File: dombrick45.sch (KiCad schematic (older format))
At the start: 5 parts

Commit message: 2019-10-04
2019-10-04 ai10さんブログの演習途中
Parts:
- added C1, C2: 22pF, Capacitor_SMD:C_0805_2012Metric, symbol Device:C_Small
- added C4, C5, C6: 0.1uF, Capacitor_SMD:C_0805_2012Metric, symbol Device:C_Small
- added C7: 10uF, Capacitor_SMD:C_0805_2012Metric, symbol Device:C_Small
- added D1, D2, D3, D4: SOD-123, Diode_SMD:D_SOD-123, symbol Device:D_Small
- added F1: 500mA, Fuse:Fuse_1206_3216Metric, symbol Device:Polyfuse_Small
- added MX1, MX2, MX3, MX4: MX-NoLED, MX_Alps_Hybrid:MX-1U-NoLED, symbol MX_Alps_Hybrid:MX-NoLED
- added R1: 10k, Resistor_SMD:R_0805_2012Metric, symbol Device:R_Small
- added SW1: SW_Push, symbol Switch:SW_Push
- added USB1: Molex-0548190589, symbol random-keyboard-parts:Molex-0548190589
- added Y1: 16MHz, symbol Device:Crystal_GND24_Small
- C3: renamed from C?; footprint (none) -> Capacitor_SMD:C_0805_2012Metric
- R2, R3, R4: renamed from R?; footprint (none) -> Resistor_SMD:R_0805_2012Metric
- gave numbers to parts that had none: 1
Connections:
- net labels added: COL0, COL1, D+, D-, ROW0, ROW1, VCC
- wire segments 13 -> 58
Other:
- moved on the sheet: R2, R3

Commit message: 2019-10-06
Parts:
- C1, C2, C3, C4, C5, C6, C7: footprint Capacitor_SMD:C_0805_2012Metric -> Capacitor_SMD:C_0805_2012Metric_Pad1.15x1.40mm_HandSolder
- SW1: footprint (none) -> random-keyboard-parts:SKQG-1155865
- USB1: footprint (none) -> random-keyboard-parts:Molex-0548190589
- Y1: footprint (none) -> Crystal:Crystal_SMD_3225-4Pin_3.2x2.5mm
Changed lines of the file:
@@
 F 0 "C3" H 2992 3271 50  0000 L CNN
 F 1 "1uF" H 2992 3180 50  0000 L CNN
-F 2 "Capacitor_SMD:C_0805_2012Metric" H 2900 3225 50  0001 C CNN
+F 2 "Capacitor_SMD:C_0805_2012Metric_Pad1.15x1.40mm_HandSolder" H 2900 3225 50  0001 C CNN
 F 3 "~" H 2900 3225 50  0001 C CNN
 	1    2900 3225
@@
 F 0 "C4" H 1892 4246 50  0000 L CNN
 F 1 "0.1uF" H 1892 4155 50  0000 L CNN
-F 2 "Capacitor_SMD:C_0805_2012Metric" H 1800 4200 50  0001 C CNN
+F 2 "Capacitor_SMD:C_0805_2012Metric_Pad1.15x1.40mm_HandSolder" H 1800 4200 50  0001 C CNN
 F 3 "~" H 1800 4200 50  0001 C CNN
 	1    1800 4200
@@
 F 0 "C5" H 2317 4246 50  0000 L CNN
 F 1 "0.1uF" H 2317 4155 50  0000 L CNN
-F 2 "Capacitor_SMD:C_0805_2012Metric" H 2225 4200 50  0001 C CNN
+F 2 "Capacitor_SMD:C_0805_2012Metric_Pad1.15x1.40mm_HandSolder" H 2225 4200 50  0001 C CNN
 F 3 "~" H 2225 4200 50  0001 C CNN
 	1    2225 4200
@@
 F 0 "C6" H 2742 4246 50  0000 L CNN
 F 1 "0.1uF" H 2742 4155 50  0000 L CNN
-F 2 "Capacitor_SMD:C_0805_2012Metric" H 2650 4200 50  0001 C CNN
+F 2 "Capacitor_SMD:C_0805_2012Metric_Pad1.15x1.40mm_HandSolder" H 2650 4200 50  0001 C CNN
 F 3 "~" H 2650 4200 50  0001 C CNN
 	1    2650 4200
@@
 F 0 "C7" H 3117 4246 50  0000 L CNN
 F 1 "10uF" H 3117 4155 50  0000 L CNN
-F 2 "Capacitor_SMD:C_0805_2012Metric" H 3025 4200 50  0001 C CNN
+F 2 "Capacitor_SMD:C_0805_2012Metric_Pad1.15x1.40mm_HandSolder" H 3025 4200 50  0001 C CNN
 F 3 "~" H 3025 4200 50  0001 C CNN
 	1    3025 4200
@@
 F 0 "SW1" H 3150 2110 50  0000 C CNN
 F 1 "SW_Push" H 3150 2019 50  0000 C CNN
-F 2 "" H 3150 2025 50  0001 C CNN
+F 2 "random-keyboard-parts:SKQG-1155865" H 3150 2025 50  0001 C CNN
 F 3 "~" H 3150 2025 50  0001 C CNN
 	1    3150 1825
@@
 F 0 "C2" V 2743 2275 50  0000 C CNN
 F 1 "22pF" V 2664 2275 50  0000 C CNN
-F 2 "Capacitor_SMD:C_0805_2012Metric" H 2550 2275 50  0001 C CNN
+F 2 "Capacitor_SMD:C_0805_2012Metric_Pad1.15x1.40mm_HandSolder" H 2550 2275 50  0001 C CNN
 F 3 "~" H 2550 2275 50  0001 C CNN
 	1    2550 2275
@@
 F 0 "C1" V 2743 1950 50  0000 C CNN
 F 1 "22pF" V 2664 1950 50  0000 C CNN
-F 2 "Capacitor_SMD:C_0805_2012Metric" H 2550 1950 50  0001 C CNN
+F 2 "Capacitor_SMD:C_0805_2012Metric_Pad1.15x1.40mm_HandSolder" H 2550 1950 50  0001 C CNN
 F 3 "~" H 2550 1950 50  0001 C CNN
 	1    2550 1950
@@
 F 0 "Y1" V 2800 2275 50  0000 L CNN
 F 1 "16MHz" V 2895 2269 50  0000 L CNN
-F 2 "" H 2850 2125 50  0001 C CNN
+F 2 "Crystal:Crystal_SMD_3225-4Pin_3.2x2.5mm" H 2850 2125 50  0001 C CNN
 F 3 "~" H 2850 2125 50  0001 C CNN
 	1    2850 2125
@@
 F 0 "USB1" V 6987 1742 60  0000 C CNN
 F 1 "Molex-0548190589" V 6881 1742 60  0000 C CNN
-F 2 "" H 6450 1775 60  0001 C CNN
+F 2 "random-keyboard-parts:Molex-0548190589" H 6450 1775 60  0001 C CNN
 F 3 "" H 6450 1775 60  0001 C CNN
 	1    6450 1775

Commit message: 2019-10-06 tutorial
hobo kansei
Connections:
- net COL0: now also U1.29 (PB5)
- net COL1: now also U1.28 (PB4)
- net ROW0: now also U1.27 (PD7)
- net ROW1: now also U1.30 (PB6)
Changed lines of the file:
@@
 $EndDescr
-$Comp
-L MCU_Microchip_ATmega:ATmega32U4-AU U1
-U 1 1 5D9215A6
-P 4025 3325
-F 0 "U1" H 4025 1436 50  0000 C CNN
-F 1 "ATmega32U4-AU" H 4025 1345 50  0000 C CNN
-F 2 "Package_QFP:TQFP-44_10x10mm_P0.8mm" H 4025 3325 50  0001 C CIN
-F 3 "http://ww1.microchip.com/downloads/en/DeviceDoc/Atmel-7766-8-bit-AVR-ATmega16U4-32U4_Datasheet.pdf" H 4025 3325 50  0001 C CNN
-	1    4025 3325
-	1    0    0    -1
-$EndComp
 $Comp
 L power:+5V #PWR0101
@@
 Text GLabel 7250 4750 0    50   Input ~ 0
 ROW1
+$Comp
+L MCU_Microchip_ATmega:ATmega32U4-AU U1
+U 1 1 5D9215A6
+P 4025 3325
+F 0 "U1" H 4025 1436 50  0000 C CNN
+F 1 "ATmega32U4-AU" H 4025 1345 50  0000 C CNN
+F 2 "Package_QFP:TQFP-44_10x10mm_P0.8mm" H 4025 3325 50  0001 C CIN
+F 3 "http://ww1.microchip.com/downloads/en/DeviceDoc/Atmel-7766-8-bit-AVR-ATmega16U4-32U4_Datasheet.pdf" H 4025 3325 50  0001 C CNN
+	1    4025 3325
+	1    0    0    -1
+$EndComp
+Text GLabel 4625 3725 2    50   Input ~ 0
+ROW0
+Text GLabel 4625 2425 2    50   Input ~ 0
+ROW1
+Text GLabel 4625 2325 2    50   Input ~ 0
+COL0
+Text GLabel 4625 2225 2    50   Input ~ 0
+COL1
 $EndSCHEMATC

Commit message: 2019-10-06 tutorial last
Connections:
- no-connect marks 0 -> 1
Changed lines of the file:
@@
 Text GLabel 4625 2225 2    50   Input ~ 0
 COL1
+NoConn ~ 6750 1475
 $EndSCHEMATC

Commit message: dombrick45 sematic to pcb tochuu
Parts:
- added D10, D11, D12, D13, D16, D17, D18, D19, D20, D21, D22, D23, D24, D25, D26, D27, D28, D29, D3, D30, D31, D32, D33, D34, D35, D36, D37, D38, D39, D4, D40, D41, D42, D43, D44, D45, D46, D47, D48, D5, D6, D7, D8, D9: SOD-123, Diode_SMD:D_SOD-123, symbol Device:D_Small
- added MX10, MX11, MX12, MX16, MX17, MX18, MX19, MX20, MX21, MX22, MX23, MX24, MX25, MX26, MX28, MX29, MX3, MX30, MX31, MX32, MX33, MX34, MX35, MX36, MX37, MX38, MX39, MX4, MX40, MX46, MX47, MX48, MX5, MX6, MX7, MX8, MX9: MX-NoLED, MX_Alps_Hybrid:MX-1U-NoLED, symbol MX_Alps_Hybrid:MX-NoLED
- added MX13, MX27, MX41, MX42, MX43, MX45: MX-NoLED, MX_Alps_Hybrid:MX-1.25U-NoLED, symbol MX_Alps_Hybrid:MX-NoLED
- added MX44: MX-NoLED, MX_Alps_Hybrid:MX-2.75U-NoLED, symbol MX_Alps_Hybrid:MX-NoLED
- MX14: renamed from MX3; footprint MX_Alps_Hybrid:MX-1U-NoLED -> MX_Alps_Hybrid:MX-1.25U-NoLED
- renumbered D3 to D14, D4 to D15, MX4 to MX15
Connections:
- net COL0: now also MX13.1 (COL), MX26.1 (COL), MX27.1 (COL), MX38.1 (COL), MX39.1 (COL), MX48.1 (COL)
- net COL1: now also MX12.1 (COL), MX25.1 (COL), MX28.1 (COL), MX40.1 (COL)
- net ROW0: now also D3.1 (K), D4.1 (K), D5.1 (K), D6.1 (K)
- net ROW1: now also D16.1 (K), D17.1 (K), D18.1 (K), D19.1 (K)
- new net: D3.2 (A), MX3.2 (ROW)
- new net: D4.2 (A), MX4.2 (ROW)
- new net: D5.2 (A), MX5.2 (ROW)
- new net: D6.2 (A), MX6.2 (ROW)
- new net: D16.2 (A), MX16.2 (ROW)
- new net: D17.2 (A), MX17.2 (ROW)
- new net: D18.2 (A), MX18.2 (ROW)
- new net: D19.2 (A), MX19.2 (ROW)
- new net: D28.2 (A), MX28.2 (ROW)
- new net: D27.2 (A), MX27.2 (ROW)
- new net: D29.2 (A), MX29.2 (ROW)
- new net: D30.2 (A), MX30.2 (ROW)
- new net: D31.2 (A), MX31.2 (ROW)
- new net: D32.2 (A), MX32.2 (ROW)
- new net: D39.2 (A), MX39.2 (ROW)
- new net: D40.2 (A), MX40.2 (ROW)
- new net: D41.2 (A), MX41.2 (ROW)
- new net: D42.2 (A), MX42.2 (ROW)
- new net: D43.2 (A), MX43.2 (ROW)
- new net: D7.2 (A), MX7.2 (ROW)
- new net: D20.2 (A), MX20.2 (ROW)
- new net: D8.2 (A), MX8.2 (ROW)
- new net: D9.2 (A), MX9.2 (ROW)
- new net: D10.2 (A), MX10.2 (ROW)
- new net: D11.2 (A), MX11.2 (ROW)
- new net: D21.2 (A), MX21.2 (ROW)
- new net: D22.2 (A), MX22.2 (ROW)
- new net: D23.2 (A), MX23.2 (ROW)
- new net: D24.2 (A), MX24.2 (ROW)
- new net: D33.2 (A), MX33.2 (ROW)
- new net: D34.2 (A), MX34.2 (ROW)
- new net: MX35.1 (COL), MX45.1 (COL)
- new net: D35.2 (A), MX35.2 (ROW)
- new net: MX36.1 (COL), MX46.1 (COL)
- new net: D36.2 (A), MX36.2 (ROW)
- new net: MX37.1 (COL), MX47.1 (COL)
- new net: D37.2 (A), MX37.2 (ROW)
- new net: D44.2 (A), MX44.2 (ROW)
- new net: D45.2 (A), MX45.2 (ROW)
- new net: D46.2 (A), MX46.2 (ROW)
- new net: D47.2 (A), MX47.2 (ROW)
- new net: D48.2 (A), MX48.2 (ROW)
- new net: D12.2 (A), MX12.2 (ROW)
- new net: D25.2 (A), MX25.2 (ROW)
- new net: D38.2 (A), MX38.2 (ROW)
- new net: D13.2 (A), MX13.2 (ROW)
- new net: D26.2 (A), MX26.2 (ROW)
- new net COL2: MX11.1 (COL), MX16.1 (COL), MX24.1 (COL), MX29.1 (COL), MX3.1 (COL), MX41.1 (COL)
- new net COL3: MX10.1 (COL), MX17.1 (COL), MX23.1 (COL), MX30.1 (COL), MX4.1 (COL), MX42.1 (COL)
- new net COL4: MX18.1 (COL), MX22.1 (COL), MX31.1 (COL), MX34.1 (COL), MX43.1 (COL), MX5.1 (COL), MX9.1 (COL)
- new net COL5: MX19.1 (COL), MX21.1 (COL), MX32.1 (COL), MX33.1 (COL), MX6.1 (COL), MX8.1 (COL)
- new net COL6: MX20.1 (COL), MX7.1 (COL)
- new net ROW2: D27.1 (K), D28.1 (K), D29.1 (K), D30.1 (K), D31.1 (K), D32.1 (K)
- new net ROW3: D39.1 (K), D40.1 (K), D41.1 (K), D42.1 (K), D43.1 (K)
- new net ROW4: D10.1 (K), D11.1 (K), D12.1 (K), D13.1 (K), D7.1 (K), D8.1 (K), D9.1 (K)
- new net ROW5: D20.1 (K), D21.1 (K), D22.1 (K), D23.1 (K), D24.1 (K), D25.1 (K), D26.1 (K)
- new net ROW6: D33.1 (K), D34.1 (K), D35.1 (K), D36.1 (K), D37.1 (K), D38.1 (K)
- new net ROW7: D44.1 (K), D45.1 (K), D46.1 (K), D47.1 (K), D48.1 (K)
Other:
- note added: "-"
- note added: "->"
- note added: "/"
- note added: ";"
- note added: "<-"
- note added: "B"
- note added: "BS"
- note added: "C"
- note added: "Cmd"
- note added: "Ctrl"
- note added: "D"
- note added: "Dombric means \nDvorak Oriented Mechanical\nBreakthough Remakable Interesting\nCoolest Keyboard :)"
- note added: "Enter"
- note added: "Esc"
- note added: "F"
- note added: "I"
- note added: "J"
- note added: "K"
- note added: "L1"
- note added: "L2"
- note added: "M"
- note added: "Option"
- note added: "Q"
- note added: "Shift"
- note added: "Space"
- note added: "T"
- note added: "Tab"
- note added: "V"
- note added: "W"
- note added: "X"
- note added: "Y"
- note added: "Z"
- note added: "down"
- note added: "up"
- moved on the sheet: C1, C2, C3, C4, C5, C6, C7, D1, D14, D15, D2, F1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

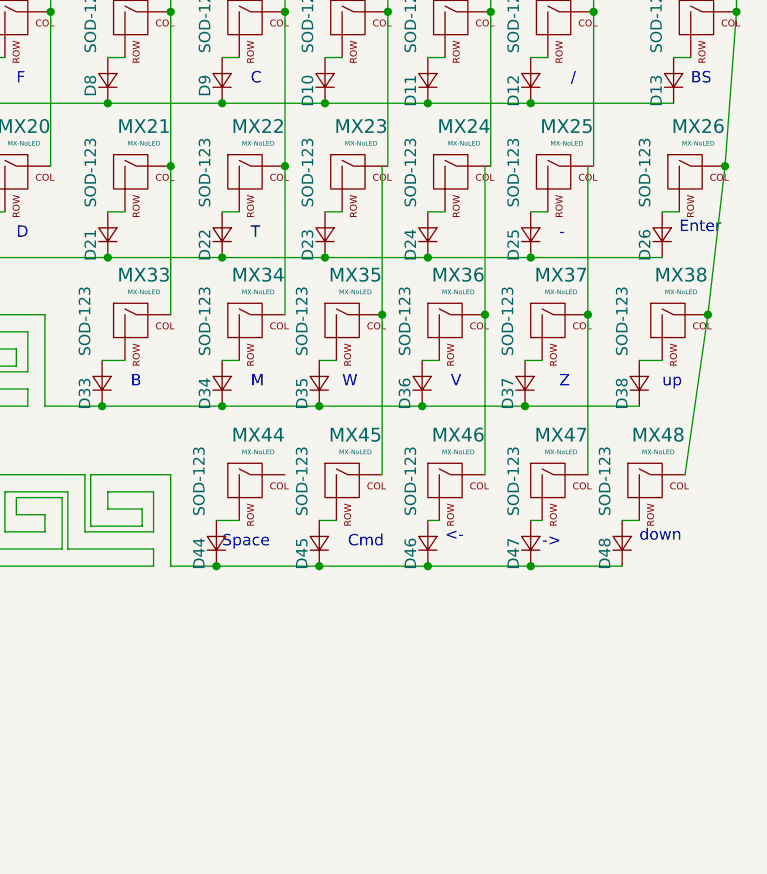
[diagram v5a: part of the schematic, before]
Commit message: 2019-10-10 keysw connect
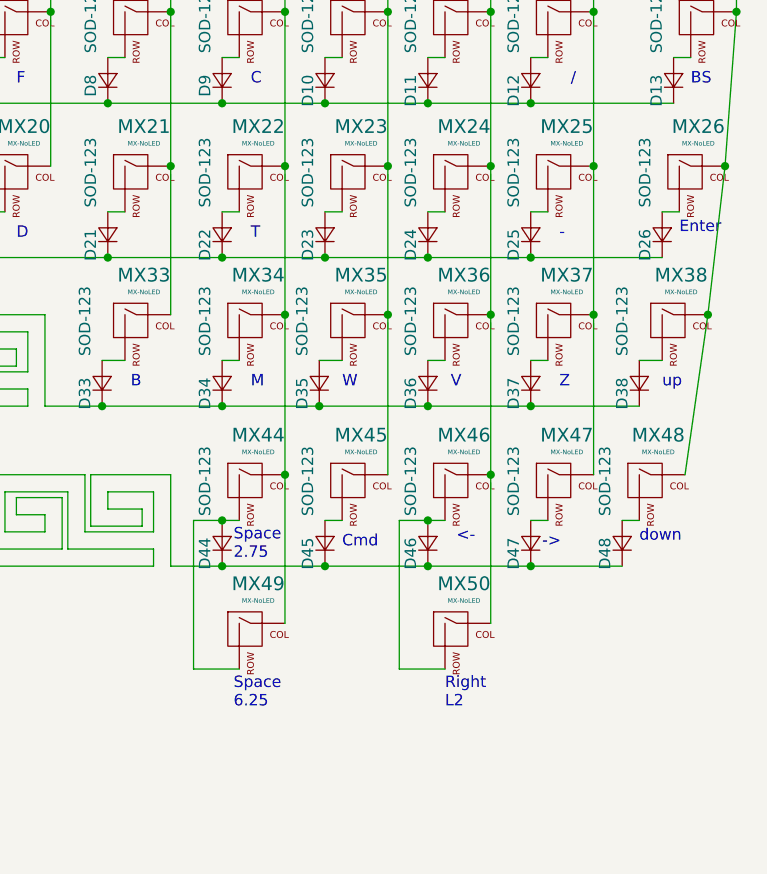
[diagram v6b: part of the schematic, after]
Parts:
- added MX49: MX-NoLED, MX_Only:MXOnly-6.25U-Hotswap, symbol MX_Alps_Hybrid:MX-NoLED
- added MX50: MX-NoLED, MX_Only:MXOnly-1.25U-Hotswap, symbol MX_Alps_Hybrid:MX-NoLED
- MX39, MX46, MX48: footprint MX_Alps_Hybrid:MX-1U-NoLED -> MX_Only:MXOnly-1U-Hotswap
- MX42, MX43, MX45: footprint MX_Alps_Hybrid:MX-1.25U-NoLED -> MX_Only:MXOnly-1.25U-Hotswap
- MX44: footprint MX_Alps_Hybrid:MX-2.75U-NoLED -> MX_Only:MXOnly-2.75U-Hotswap-ReversedStabilizers
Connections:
- net COL1: now also MX37.1 (COL), MX47.1 (COL)
- net COL2: now also MX36.1 (COL), MX46.1 (COL), MX50.1 (COL)
- net COL3: now also MX35.1 (COL), MX45.1 (COL)
- net COL4: now also MX44.1 (COL), MX49.1 (COL)
- net at D44.2 (A), MX44.2 (ROW): now also MX49.2 (ROW)
- net at D46.2 (A), MX46.2 (ROW): now also MX50.2 (ROW)
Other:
- note added: "Right\nL2"
- note added: "Space\n2.75"
- note added: "Space\n6.25"
- note removed: "Space"
- moved on the sheet: D36, D37, D44, D45, MX35, MX36, MX37, MX45, MX46, MX47

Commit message: 2019-10-12 PBC ver0.1
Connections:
- net COL0: now also U1.18 (PD0); no longer U1.29 (PB5)
- net COL1: now also U1.21 (PD3); no longer U1.28 (PB4)
- net COL2: now also U1.31 (PC6)
- net COL3: now also U1.30 (PB6)
- net COL4: now also U1.29 (PB5)
- net COL5: now also U1.28 (PB4)
- net COL6: now also U1.37 (PF6)
- net ROW0: now also U1.36 (PF7); no longer U1.27 (PD7)
- net ROW1: now also U1.32 (PC7); no longer U1.30 (PB6)
- net ROW2: now also U1.27 (PD7)
- net ROW3: now also U1.26 (PD6)
- net ROW4: now also U1.39 (PF4)
- net ROW5: now also U1.38 (PF5)
- net ROW6: now also U1.19 (PD1)
- net ROW7: now also U1.20 (PD2)
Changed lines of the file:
@@
 Text GLabel 3875 2325 0    50   Input ~ 0
 ROW1
-Text GLabel 2925 3250 2    50   Input ~ 0
-ROW0
-Text GLabel 2925 1950 2    50   Input ~ 0
-ROW1
-Text GLabel 2925 1850 2    50   Input ~ 0
-COL0
-Text GLabel 2925 1750 2    50   Input ~ 0
-COL1
 NoConn ~ 2125 6200
 Text GLabel 875  2450 0    50   Input ~ 0
@@
 Wire Wire Line
 	9200 3675 9650 3675
+Text GLabel 2925 4250 2    50   Input ~ 0
+ROW0
+Text GLabel 2925 4150 2    50   Input ~ 0
+COL6
+Text GLabel 2925 4050 2    50   Input ~ 0
+ROW5
+Text GLabel 2925 3950 2    50   Input ~ 0
+ROW4
+Text GLabel 2925 2350 2    50   Input ~ 0
+ROW1
+Text GLabel 2925 2250 2    50   Input ~ 0
+COL2
+Text GLabel 2925 1950 2    50   Input ~ 0
+COL3
+Text GLabel 2925 1850 2    50   Input ~ 0
+COL4
+Text GLabel 2925 1750 2    50   Input ~ 0
+COL5
+Text GLabel 2925 3250 2    50   Input ~ 0
+ROW2
+Text GLabel 2925 3150 2    50   Input ~ 0
+ROW3
+Text GLabel 2925 2850 2    50   Input ~ 0
+COL1
+Text GLabel 2925 2750 2    50   Input ~ 0
+ROW7
+Text GLabel 2925 2650 2    50   Input ~ 0
+ROW6
+Text GLabel 2925 2550 2    50   Input ~ 0
+COL0
 $EndSCHEMATC

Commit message: 2019-10-14 SPI toridashi and dombri mark
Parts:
- added J1: AVR-ISP-6, random-keyboard-parts:Reset_Pretty, symbol Connector:AVR-ISP-6
- MX40, MX47: footprint MX_Alps_Hybrid:MX-1U-NoLED -> MX_Only:MXOnly-1U-Hotswap
- MX41: footprint MX_Alps_Hybrid:MX-1.25U-NoLED -> MX_Only:MXOnly-1.25U-Hotswap
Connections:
- net +5V: now also J1.2 (VCC)
- net GND: now also J1.6 (GND)
- net at U1.10 (PB2): now also J1.4 (MOSI)
- net at U1.11 (PB3): now also J1.1 (MISO)
- net RESET: now reaches R1.1, SW1.2, U1.13 (~RESET)
- net RESET: now also J1.5 (~RST)
- net at U1.9 (PB1): now also J1.3 (SCK)
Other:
- moved on the sheet: D1, D10, D11, D12, D13, D14, D15, D16, D17, D18, D19, D2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
